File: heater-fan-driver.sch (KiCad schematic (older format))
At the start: 15 parts

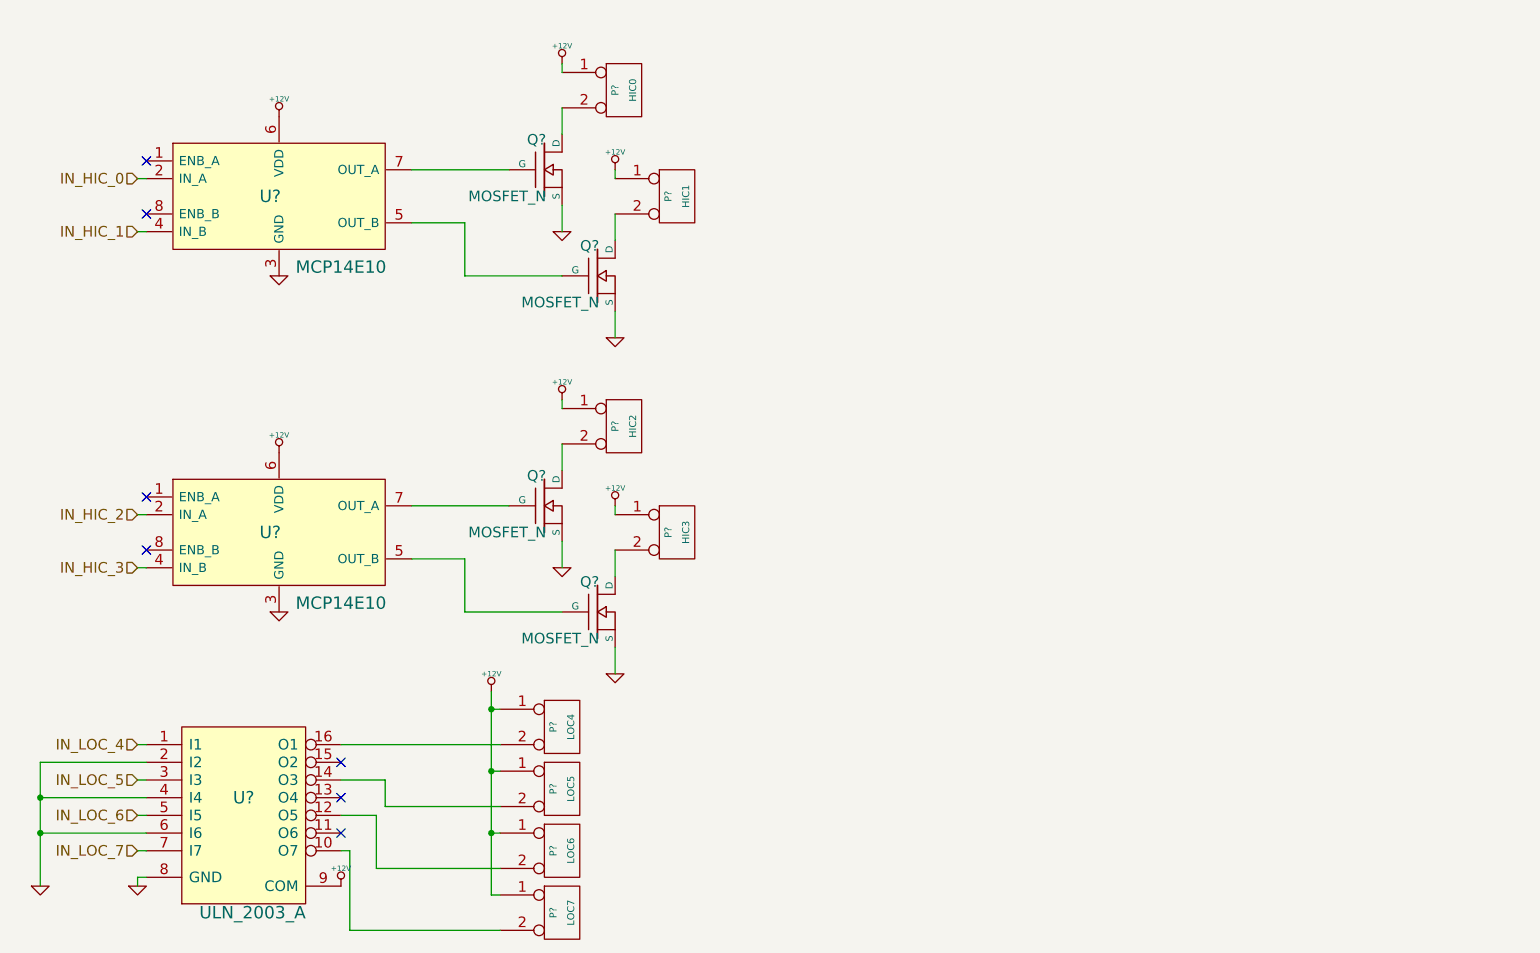
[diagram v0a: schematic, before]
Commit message: Added signal LEDs to hi-current and lo-current drivers, updated BOM
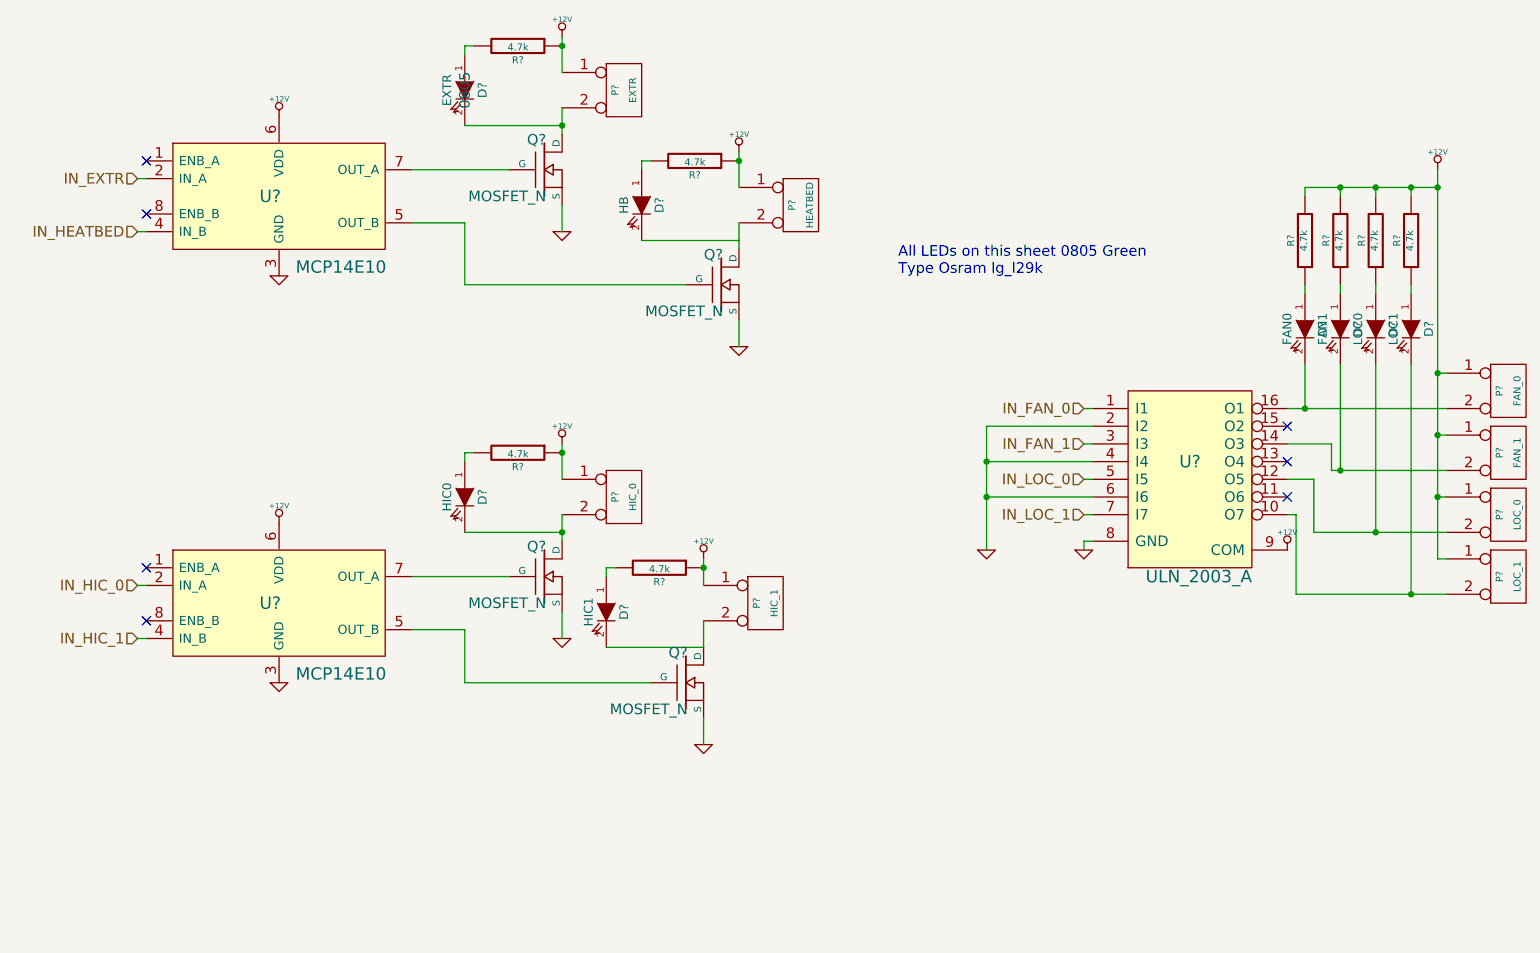
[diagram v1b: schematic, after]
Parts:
- added D?: EXTR, 0805, symbol LED
- added D?: HB, symbol LED
- added D?: HIC0, symbol LED
- added D?: HIC1, symbol LED
- added D?: LOC1, symbol LED
- added D?: LOC0, symbol LED
- added D?: FAN1, symbol LED
- added D?: FAN0, symbol LED
- added R? (x8): 4.7k, symbol R
- P?: value HIC0 -> EXTR
- P?: value HIC1 -> HEATBED
- P?: value HIC2 -> HIC_0
- P?: value HIC3 -> HIC_1
- P?: value LOC4 -> FAN_0
- P?: value LOC5 -> FAN_1
- P?: value LOC6 -> LOC_0
- P?: value LOC7 -> LOC_1
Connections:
- net IN_HIC_2 is gone; now on net IN_HIC_0: U?.2 (IN_A)
- net IN_HIC_3 is gone; now on net IN_HIC_1: U?.4 (IN_B)
- net +12V: now also R?.1, R?.1, R?.1, R?.1, R?.2, R?.2, R?.2, R?.2
- net IN_HIC_0: no longer U?.2 (IN_A)
- net IN_HIC_1: no longer U?.4 (IN_B)
- net at P?.2 (PM), Q?.D: now also D?.2 (K) (x3)
- net at P?.2 (PM), U?.10 (O7): now also D?.2 (K)
- net at P?.2 (PM), U?.12 (O5): now also D?.2 (K)
- net at P?.2 (PM), U?.14 (O3): now also D?.2 (K)
- net at P?.2 (PM), U?.16 (O1): now also D?.2 (K)
- net IN_LOC_4 renamed IN_FAN_0
- net IN_LOC_5 renamed IN_FAN_1
- net IN_LOC_6 renamed IN_LOC_0
- net IN_LOC_7 renamed IN_LOC_1
- new net: D?.1 (A), R?.2 (x4)
- new net: D?.1 (A), R?.1 (x4)
- new net IN_EXTR: U?.2 (IN_A)
- new net IN_HEATBED: U?.4 (IN_B)
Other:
- note added: "All LEDs on this sheet 0805 Green\nType Osram lg_l29k\n"
- moved on the sheet: P?, Q?, U?

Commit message: Added potentiometer to make beeper volume adjustable
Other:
- note added: "All LEDs on this sheet 0603 Green\nType Osram lg_l29k\n"
- note removed: "All LEDs on this sheet 0805 Green\nType Osram lg_l29k\n"
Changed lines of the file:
@@
 encoding utf-8
 Sheet 3 3
-Title ""
+Title "Fan and Heater drivers"
 Date ""
-Rev ""
+Rev "A"
 Comp ""
-Comment1 ""
+Comment1 "4 High-Current Channels (Heaters), 4 Low-C.-Ch. (Fans)"
 Comment2 ""
 Comment3 ""
@@
 	8100 4600 7950 4600
 Text Notes 5750 3450 0    60   ~ 0
-All LEDs on this sheet 0805 Green\nType Osram lg_l29k\n
+All LEDs on this sheet 0603 Green\nType Osram lg_l29k\n
 $EndSCHEMATC

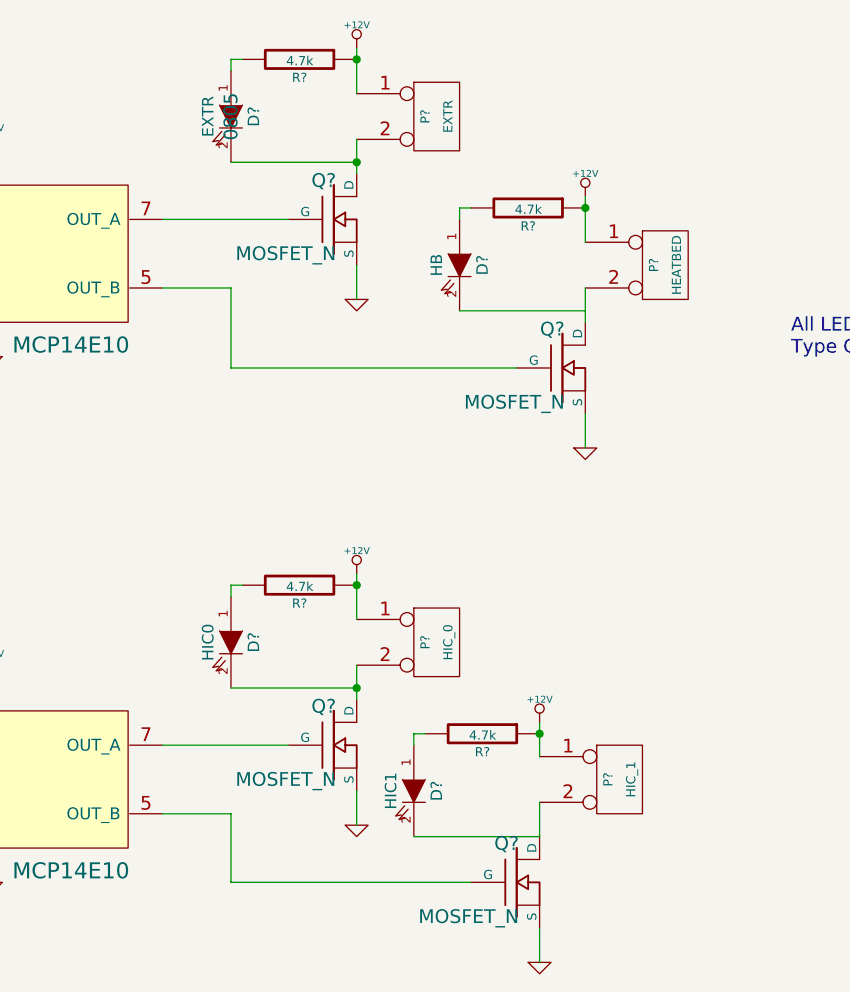
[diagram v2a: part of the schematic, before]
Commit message: Added protection diodes for heater drivers Added pcb file (empty yet)
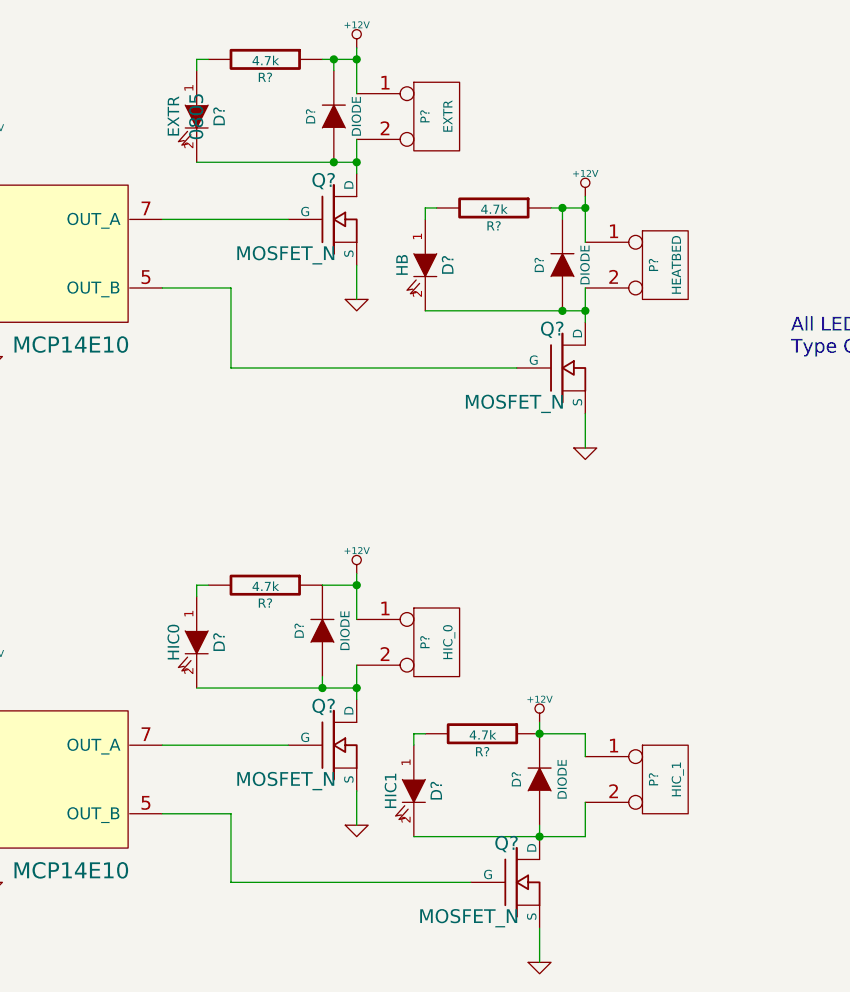
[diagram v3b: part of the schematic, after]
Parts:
- added D? (x4): DIODE, symbol DIODE
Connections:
- net +12V: now also D?.2 (K), D?.2 (K), D?.2 (K), D?.2 (K)
- net at D?.2 (K), P?.2 (PM), Q?.D: now also D?.1 (A) (x3)
- net at P?.2 (PM), Q?.D: now also D?.2 (K), D?.1 (A)
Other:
- moved on the sheet: D?, P?, R?
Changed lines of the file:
@@
 $EndComp
-Wire Wire Line
-	3850 2100 3850 2300
 Wire Wire Line
 	3550 2850 3000 2850
@@
 L CONN_2 P?
 U 1 1 534EC16C
-P 5000 5300
-F 0 "P?" V 4950 5300 40  0000 C CNN
-F 1 "HIC_1" V 5050 5300 40  0000 C CNN
-F 2 "" H 5000 5300 60  0000 C CNN
-F 3 "" H 5000 5300 60  0000 C CNN
-	1    5000 5300
+P 5200 5300
+F 0 "P?" V 5150 5300 40  0000 C CNN
+F 1 "HIC_1" V 5250 5300 40  0000 C CNN
+F 2 "" H 5200 5300 60  0000 C CNN
+F 3 "" H 5200 5300 60  0000 C CNN
+	1    5200 5300
 	1    0    0    -1
 $EndComp
@@
 Wire Wire Line
 	4650 6100 4650 5950
-Wire Wire Line
-	4650 5400 4650 5550
 $Comp
 L +12V #PWR?
@@
 	1    0    0    -1
 $EndComp
-Wire Wire Line
-	4650 5050 4650 5200
 Wire Wire Line
 	3300 5750 4350 5750
@@
 L LED D?
 U 1 1 53500700
-P 3300 2400
-F 0 "D?" H 3300 2500 50  0000 C CNN
-F 1 "EXTR" H 3300 2300 50  0000 C CNN
-F 2 "0805" H 3300 2400 60  0000 C CNN
-F 3 "" H 3300 2400 60  0000 C CNN
-F 4 "lg_l29k" H 3300 2400 60  0001 C CNN "Model"
-	1    3300 2400
+P 3150 2400
+F 0 "D?" H 3150 2500 50  0000 C CNN
+F 1 "EXTR" H 3150 2300 50  0000 C CNN
+F 2 "0805" H 3150 2400 60  0000 C CNN
+F 3 "" H 3150 2400 60  0000 C CNN
+F 4 "lg_l29k" H 3150 2400 60  0001 C CNN "Model"
+	1    3150 2400
 	0    1    1    0
 $EndComp
@@
 L R R?
 U 1 1 53500760
-P 3600 2150
-F 0 "R?" V 3680 2150 40  0000 C CNN
-F 1 "4.7k" V 3607 2151 40  0000 C CNN
-F 2 "" V 3530 2150 30  0000 C CNN
-F 3 "" H 3600 2150 30  0000 C CNN
-	1    3600 2150
-	0    1    1    0
-$EndComp
-Wire Wire Line
-	3350 2150 3300 2150
-Wire Wire Line
-	3300 2150 3300 2200
-Wire Wire Line
-	3300 2600 3850 2600
+P 3450 2150
+F 0 "R?" V 3530 2150 40  0000 C CNN
+F 1 "4.7k" V 3457 2151 40  0000 C CNN
+F 2 "" V 3380 2150 30  0000 C CNN
+F 3 "" H 3450 2150 30  0000 C CNN
+	1    3450 2150
+	0    1    1    0
+$EndComp
+Wire Wire Line
+	3200 2150 3150 2150
+Wire Wire Line
+	3150 2150 3150 2200
+Wire Wire Line
+	3150 2600 3850 2600
 Connection ~ 3850 2600
 $Comp
 L LED D?
 U 1 1 535007F1
-P 4300 3050
-F 0 "D?" H 4300 3150 50  0000 C CNN
-F 1 "HB" H 4300 2950 50  0000 C CNN
-F 2 "" H 4300 3050 60  0000 C CNN
-F 3 "" H 4300 3050 60  0000 C CNN
-	1    4300 3050
+P 4150 3050
+F 0 "D?" H 4150 3150 50  0000 C CNN
+F 1 "HB" H 4150 2950 50  0000 C CNN
+F 2 "" H 4150 3050 60  0000 C CNN
+F 3 "" H 4150 3050 60  0000 C CNN
+	1    4150 3050
 	0    1    1    0
 $EndComp
@@
 L R R?
 U 1 1 535007F7
-P 4600 2800
-F 0 "R?" V 4680 2800 40  0000 C CNN
-F 1 "4.7k" V 4607 2801 40  0000 C CNN
-F 2 "" V 4530 2800 30  0000 C CNN
-F 3 "" H 4600 2800 30  0000 C CNN
-	1    4600 2800
-	0    1    1    0
-$EndComp
-Wire Wire Line
-	4350 2800 4300 2800
-Wire Wire Line
-	4300 2800 4300 2850
-Wire Wire Line
-	4300 3250 4850 3250
+P 4450 2800
+F 0 "R?" V 4530 2800 40  0000 C CNN
+F 1 "4.7k" V 4457 2801 40  0000 C CNN
+F 2 "" V 4380 2800 30  0000 C CNN
+F 3 "" H 4450 2800 30  0000 C CNN
+	1    4450 2800
+	0    1    1    0
+$EndComp
+Wire Wire Line
+	4200 2800 4150 2800
+Wire Wire Line
+	4150 2800 4150 2850
+Wire Wire Line
+	4150 3250 4850 3250
 Connection ~ 4850 2800
 Wire Wire Line
@@
 L LED D?
 U 1 1 535008DF
-P 3300 4700
-F 0 "D?" H 3300 4800 50  0000 C CNN
-F 1 "HIC0" H 3300 4600 50  0000 C CNN
-F 2 "" H 3300 4700 60  0000 C CNN
-F 3 "" H 3300 4700 60  0000 C CNN
-	1    3300 4700
+P 3150 4700
+F 0 "D?" H 3150 4800 50  0000 C CNN
+F 1 "HIC0" H 3150 4600 50  0000 C CNN
+F 2 "" H 3150 4700 60  0000 C CNN
+F 3 "" H 3150 4700 60  0000 C CNN
+	1    3150 4700
 	0    1    1    0
 $EndComp
@@
 L R R?
 U 1 1 535008E5
-P 3600 4450
-F 0 "R?" V 3680 4450 40  0000 C CNN
-F 1 "4.7k" V 3607 4451 40  0000 C CNN
-F 2 "" V 3530 4450 30  0000 C CNN
-F 3 "" H 3600 4450 30  0000 C CNN
-	1    3600 4450
-	0    1    1    0
-$EndComp
-Wire Wire Line
-	3350 4450 3300 4450
-Wire Wire Line
-	3300 4450 3300 4500
-Wire Wire Line
-	3300 4900 3850 4900
+P 3450 4450
+F 0 "R?" V 3530 4450 40  0000 C CNN
+F 1 "4.7k" V 3457 4451 40  0000 C CNN
+F 2 "" V 3380 4450 30  0000 C CNN
+F 3 "" H 3450 4450 30  0000 C CNN
+	1    3450 4450
+	0    1    1    0
+$EndComp
+Wire Wire Line
+	3200 4450 3150 4450
+Wire Wire Line
+	3150 4450 3150 4500
+Wire Wire Line
+	3150 4900 3850 4900
 Connection ~ 3850 4450
 $Comp
@@
 	4100 5100 4100 5150
 Wire Wire Line
-	4650 5550 4100 5550
+	4850 5550 4100 5550
 Connection ~ 4650 5100
 Connection ~ 3850 2150
-Connection ~ 3850 4900
 $Comp
 L LED D?
@@
 Text Notes 5750 3450 0    60   ~ 0
 All LEDs on this sheet 0603 Green\nType Osram lg_l29k\n
+$Comp
+L DIODE D?
+U 1 1 535114A1
+P 3700 4650
+F 0 "D?" H 3700 4750 40  0000 C CNN
+F 1 "DIODE" H 3700 4550 40  0000 C CNN
+F 2 "" H 3700 4650 60  0000 C CNN
+F 3 "" H 3700 4650 60  0000 C CNN
+	1    3700 4650
+	0    -1   -1   0
+$EndComp
+Wire Wire Line
+	3700 4900 3700 4850
+$Comp
+L DIODE D?
+U 1 1 535115D5
+P 3750 2400
+F 0 "D?" H 3750 2500 40  0000 C CNN
+F 1 "DIODE" H 3750 2300 40  0000 C CNN
+F 2 "" H 3750 2400 60  0000 C CNN
+F 3 "" H 3750 2400 60  0000 C CNN
+	1    3750 2400
+	0    -1   -1   0
+$EndComp
+Wire Wire Line
+	3700 2150 3850 2150
+Wire Wire Line
+	3750 2200 3750 2150
+Connection ~ 3750 2150
+Connection ~ 3750 2600
+Wire Wire Line
+	3850 2100 3850 2300
+$Comp
+L DIODE D?
+U 1 1 53511841
+P 4750 3050
+F 0 "D?" H 4750 3150 40  0000 C CNN
+F 1 "DIODE" H 4750 2950 40  0000 C CNN
+F 2 "" H 4750 3050 60  0000 C CNN
+F 3 "" H 4750 3050 60  0000 C CNN
+	1    4750 3050
+	0    -1   -1   0
+$EndComp
+Wire Wire Line
+	4700 2800 4850 2800
+Wire Wire Line
+	4750 2850 4750 2800
+Connection ~ 4750 2800
+Connection ~ 4850 3250
+Connection ~ 4750 3250
+Wire Wire Line
+	3700 4450 3850 4450
+Connection ~ 3850 4900
+Connection ~ 3700 4900
+$Comp
+L DIODE D?
+U 1 1 53511B29
+P 4650 5300
+F 0 "D?" H 4650 5400 40  0000 C CNN
+F 1 "DIODE" H 4650 5200 40  0000 C CNN
+F 2 "" H 4650 5300 60  0000 C CNN
+F 3 "" H 4650 5300 60  0000 C CNN
+	1    4650 5300
+	0    -1   -1   0
+$EndComp
+Wire Wire Line
+	4650 5500 4650 5550
+Wire Wire Line
+	4650 5100 4850 5100
+Connection ~ 4650 5550
+Wire Wire Line
+	4650 5100 4650 5050
+Wire Wire Line
+	4850 5100 4850 5200
+Wire Wire Line
+	4850 5400 4850 5550
 $EndSCHEMATC
